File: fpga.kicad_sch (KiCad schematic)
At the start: 0 parts

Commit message: Chose amplifiers
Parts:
- added U10: P0082_TOPMOUNT, P0082_TOPMOUNT:MODULE_P0082_TOPMOUNT, symbol P0082_TOPMOUNT:P0082_TOPMOUNT
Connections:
- new net: U10.S1 (SHIELD), U10.S2 (SHIELD), U10.S3 (SHIELD), U10.S4 (SHIELD)

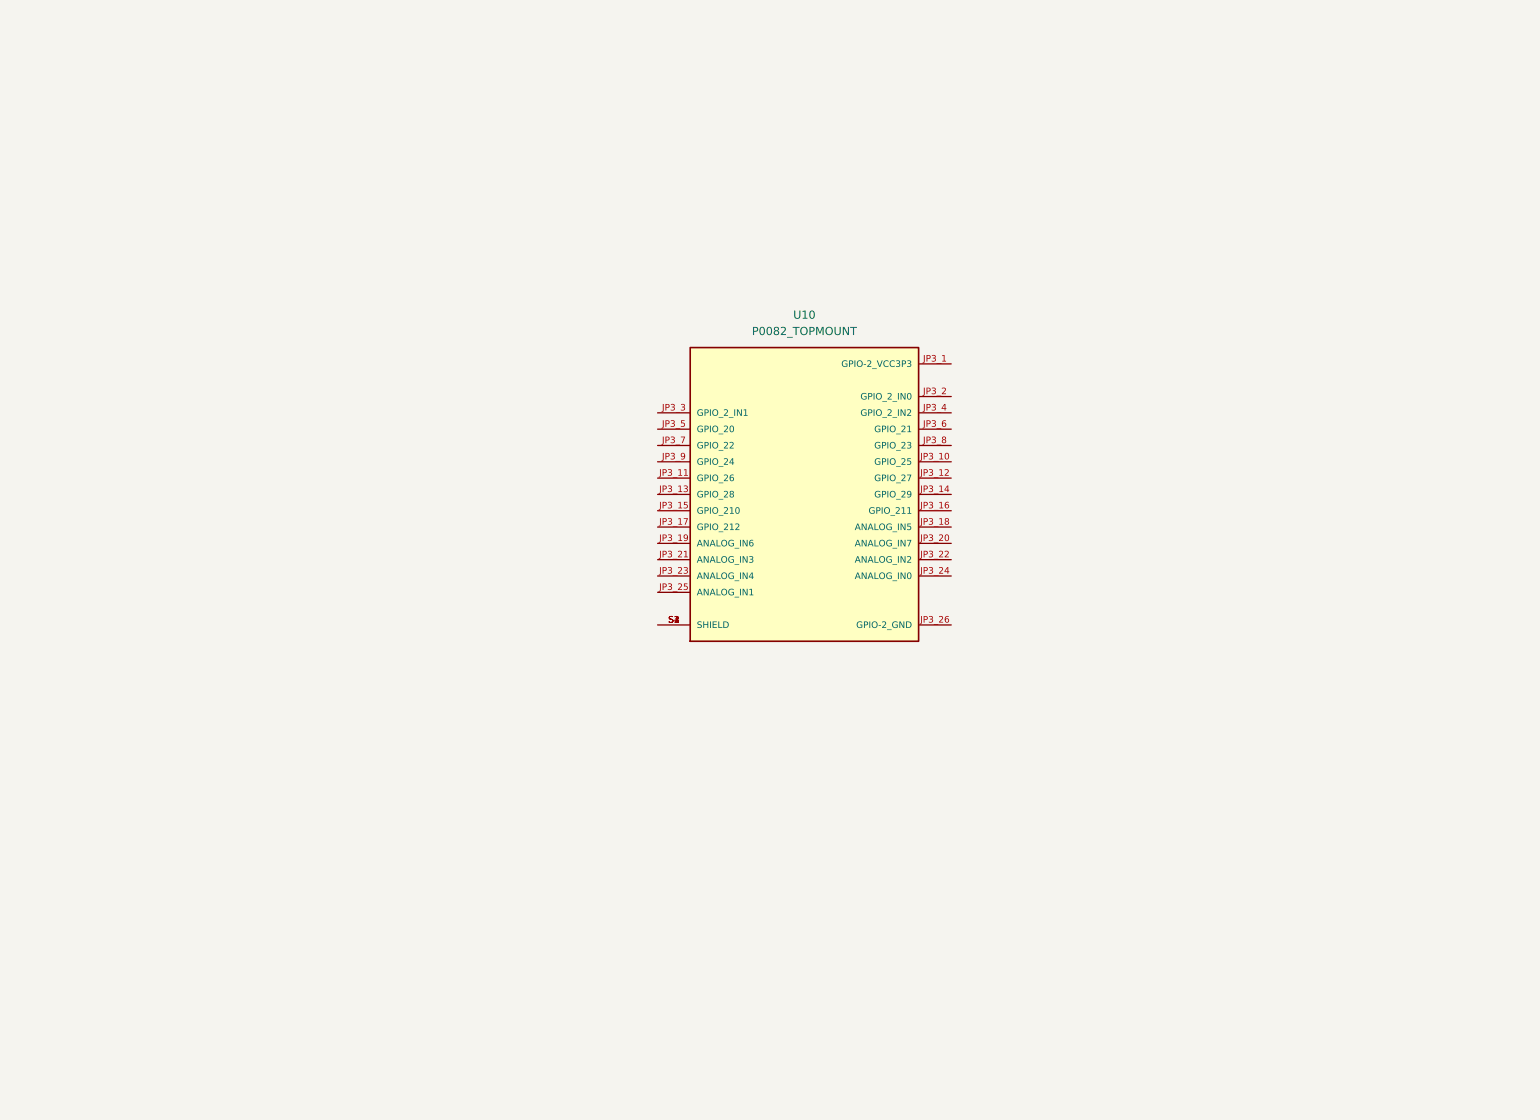
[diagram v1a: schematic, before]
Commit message: Add some of the AF power supply levels
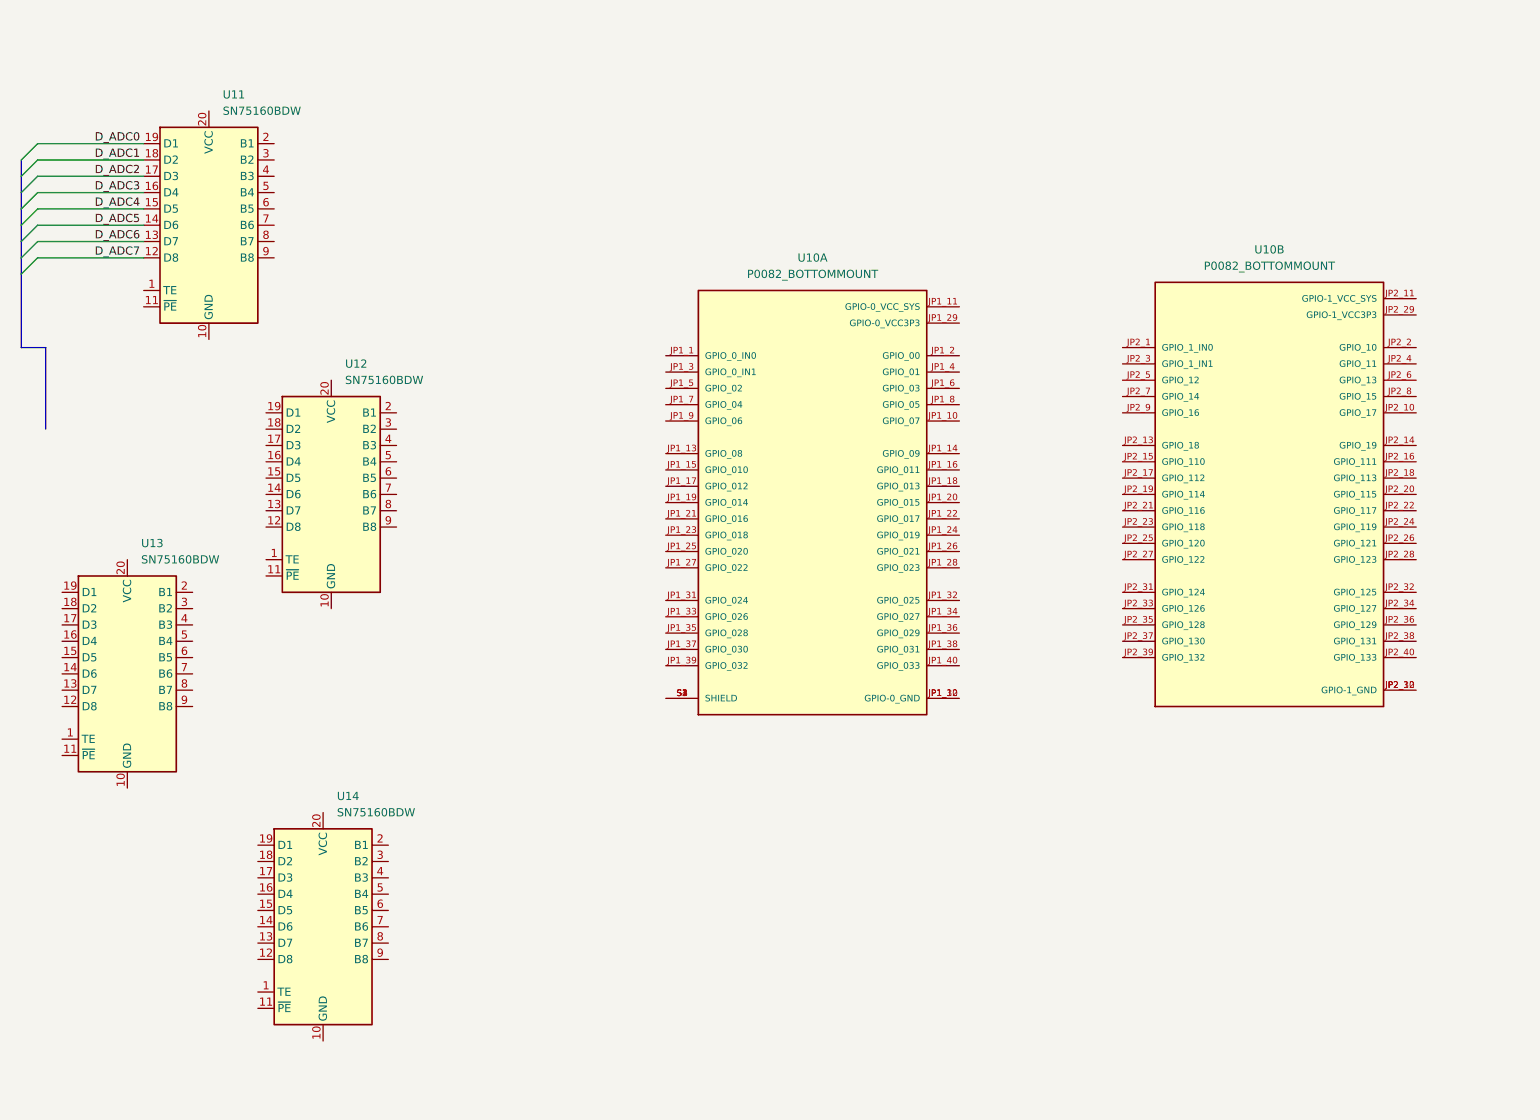
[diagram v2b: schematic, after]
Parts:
- removed U10: P0082_TOPMOUNT, P0082_TOPMOUNT:MODULE_P0082_TOPMOUNT, symbol P0082_TOPMOUNT:P0082_TOPMOUNT
- added U10: P0082_BOTTOMMOUNT, P0082_BOTTOMMOUNT:MODULE_P0082_BOTTOMMOUNT, symbol P0082_BOTTOMMOUNT:P0082_BOTTOMMOUNT
- added U11, U12, U13, U14: SN75160BDW, Package_SO:SOIC-20W_7.5x12.8mm_P1.27mm, symbol Interface:SN75160BDW
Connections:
- new net: U10.JP1_12 (GPIO-0_GND), U10.JP1_30 (GPIO-0_GND)
- new net: U10.S1 (SHIELD), U10.S2 (SHIELD), U10.S3 (SHIELD), U10.S4 (SHIELD)
- new net: U10.JP2_12 (GPIO-1_GND), U10.JP2_30 (GPIO-1_GND)
- new net D_ADC0: U11.19 (D1)
- new net D_ADC1: U11.18 (D2)
- new net D_ADC2: U11.17 (D3)
- new net D_ADC3: U11.16 (D4)
- new net D_ADC4: U11.15 (D5)
- new net D_ADC5: U11.14 (D6)
- new net D_ADC6: U11.13 (D7)
- new net D_ADC7: U11.12 (D8)

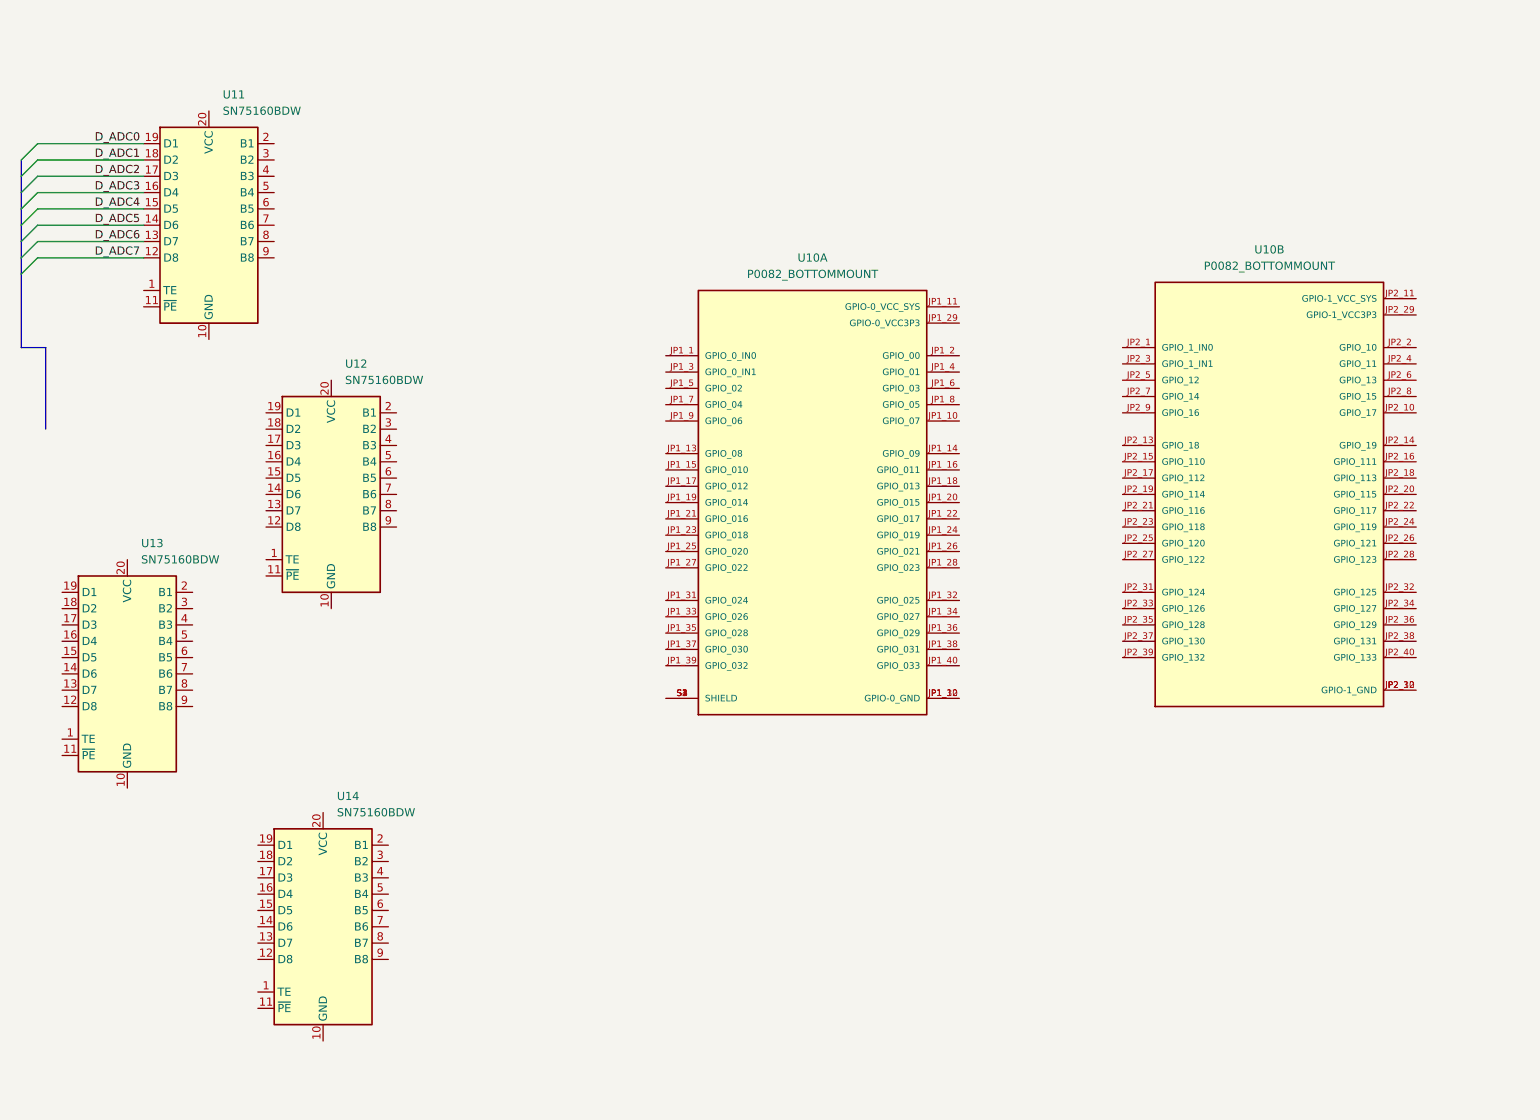
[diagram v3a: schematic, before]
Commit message: Link up ADC to FPGA
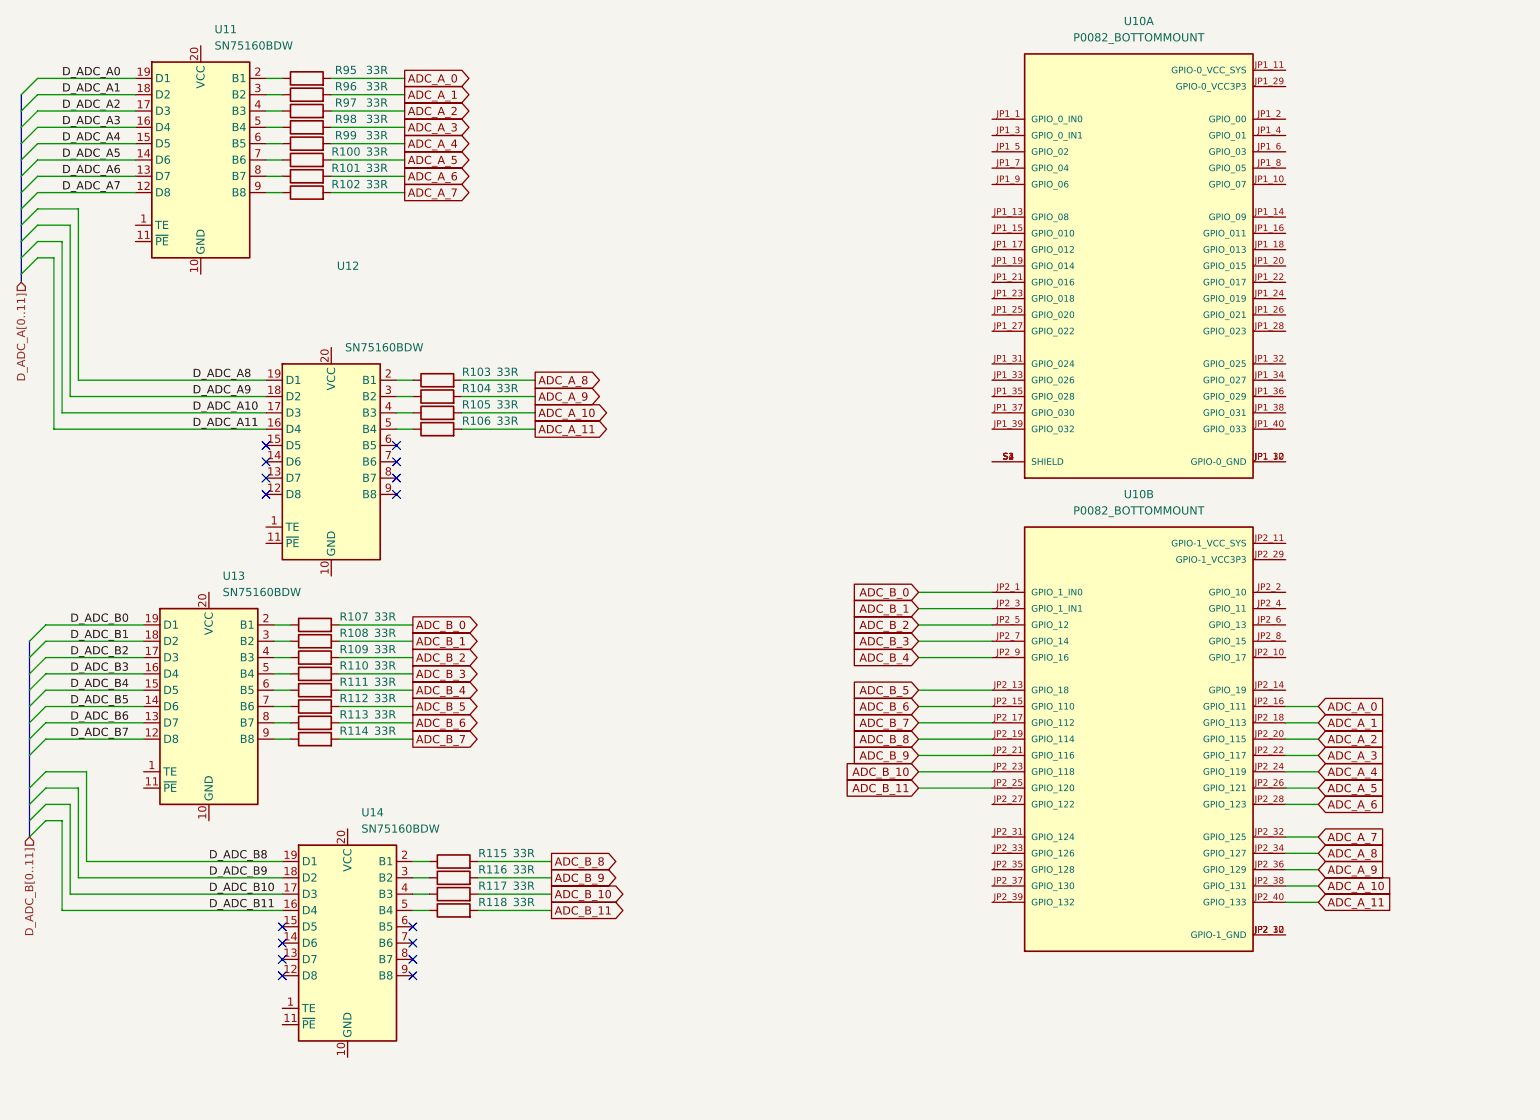
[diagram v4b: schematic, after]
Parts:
- added R100, R101, R102, R103, R104, R105, R106, R107, R108, R109, R110, R111, R112, R113, R114, R115, R116, R117, R118, R95, R96, R97, R98, R99: 33R, Resistor_SMD:R_0402_1005Metric_Pad0.72x0.64mm_HandSolder, symbol Device:R
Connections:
- net D_ADC_A11: now reaches U12.16 (D4)
- net D_ADC_A10: now reaches U12.17 (D3)
- net D_ADC_A9: now reaches U12.18 (D2)
- net D_ADC_A8: now reaches U12.19 (D1)
- net at U12.2 (B1): now also R103.1
- net at U12.3 (B2): now also R104.1
- net at U12.4 (B3): now also R105.1
- net at U12.5 (B4): now also R106.1
- net at U11.2 (B1): now also R95.1
- net at U11.3 (B2): now also R96.1
- net at U11.4 (B3): now also R97.1
- net at U11.5 (B4): now also R98.1
- net at U11.6 (B5): now also R99.1
- net at U11.7 (B6): now also R100.1
- net at U11.8 (B7): now also R101.1
- net at U11.9 (B8): now also R102.1
- net D_ADC_B7: now reaches U13.12 (D8)
- net D_ADC_B6: now reaches U13.13 (D7)
- net D_ADC_B5: now reaches U13.14 (D6)
- net D_ADC_B4: now reaches U13.15 (D5)
- net D_ADC_B3: now reaches U13.16 (D4)
- net D_ADC_B2: now reaches U13.17 (D3)
- net D_ADC_B1: now reaches U13.18 (D2)
- net D_ADC_B0: now reaches U13.19 (D1)
- net at U13.2 (B1): now also R107.1
- net at U13.3 (B2): now also R108.1
- net at U13.4 (B3): now also R109.1
- net at U13.5 (B4): now also R110.1
- net at U13.6 (B5): now also R111.1
- net at U13.7 (B6): now also R112.1
- net at U13.8 (B7): now also R113.1
- net at U13.9 (B8): now also R114.1
- net D_ADC_B11: now reaches U14.16 (D4)
- net D_ADC_B10: now reaches U14.17 (D3)
- net D_ADC_B9: now reaches U14.18 (D2)
- net D_ADC_B8: now reaches U14.19 (D1)
- net at U14.2 (B1): now also R115.1
- net at U14.3 (B2): now also R116.1
- net at U14.4 (B3): now also R117.1
- net at U14.5 (B4): now also R118.1
- net ADC_B_0: now reaches U10.JP2_1 (GPIO_1_IN0)
- net ADC_B_0: now also R107.2
- net ADC_B_5: now reaches U10.JP2_13 (GPIO_18)
- net ADC_B_5: now also R112.2
- net ADC_B_6: now reaches U10.JP2_15 (GPIO_110)
- net ADC_B_6: now also R113.2
- net ADC_A_0: now reaches U10.JP2_16 (GPIO_111)
- net ADC_A_0: now also R95.2
- net ADC_B_7: now reaches U10.JP2_17 (GPIO_112)
- net ADC_B_7: now also R114.2
- net ADC_A_1: now reaches U10.JP2_18 (GPIO_113)
- net ADC_A_1: now also R96.2
- net ADC_B_8: now reaches U10.JP2_19 (GPIO_114)
- net ADC_B_8: now also R115.2
- net ADC_A_2: now reaches U10.JP2_20 (GPIO_115)
- net ADC_A_2: now also R97.2
- net ADC_B_9: now reaches U10.JP2_21 (GPIO_116)
- net ADC_B_9: now also R116.2
- net ADC_A_3: now reaches U10.JP2_22 (GPIO_117)
- net ADC_A_3: now also R98.2
- net ADC_B_10: now reaches U10.JP2_23 (GPIO_118)
- net ADC_B_10: now also R117.2
- net ADC_A_4: now reaches U10.JP2_24 (GPIO_119)
- net ADC_A_4: now also R99.2
- net ADC_B_11: now reaches U10.JP2_25 (GPIO_120)
- net ADC_B_11: now also R118.2
- net ADC_A_5: now reaches U10.JP2_26 (GPIO_121)
- net ADC_A_5: now also R100.2
- net ADC_A_6: now reaches U10.JP2_28 (GPIO_123)
- net ADC_A_6: now also R101.2
- net ADC_B_1: now reaches U10.JP2_3 (GPIO_1_IN1)
- net ADC_B_1: now also R108.2
- net ADC_A_7: now reaches U10.JP2_32 (GPIO_125)
- net ADC_A_7: now also R102.2
- net ADC_A_8: now reaches U10.JP2_34 (GPIO_127)
- net ADC_A_8: now also R103.2
- net ADC_A_9: now reaches U10.JP2_36 (GPIO_129)
- net ADC_A_9: now also R104.2
- net ADC_A_10: now reaches U10.JP2_38 (GPIO_131)
- net ADC_A_10: now also R105.2
- net ADC_A_11: now reaches U10.JP2_40 (GPIO_133)
- net ADC_A_11: now also R106.2
- net ADC_B_2: now reaches U10.JP2_5 (GPIO_12)
- net ADC_B_2: now also R109.2
- net ADC_B_3: now reaches U10.JP2_7 (GPIO_14)
- net ADC_B_3: now also R110.2
- net ADC_B_4: now reaches U10.JP2_9 (GPIO_16)
- net ADC_B_4: now also R111.2
- net D_ADC0 renamed D_ADC_A0
- net D_ADC1 renamed D_ADC_A1
- net D_ADC2 renamed D_ADC_A2
- net D_ADC3 renamed D_ADC_A3
- net D_ADC4 renamed D_ADC_A4
- net D_ADC5 renamed D_ADC_A5
- net D_ADC6 renamed D_ADC_A6
- net D_ADC7 renamed D_ADC_A7
- no-connect marks 0 -> 16
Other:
- moved on the sheet: U10A, U10B, U11, U12

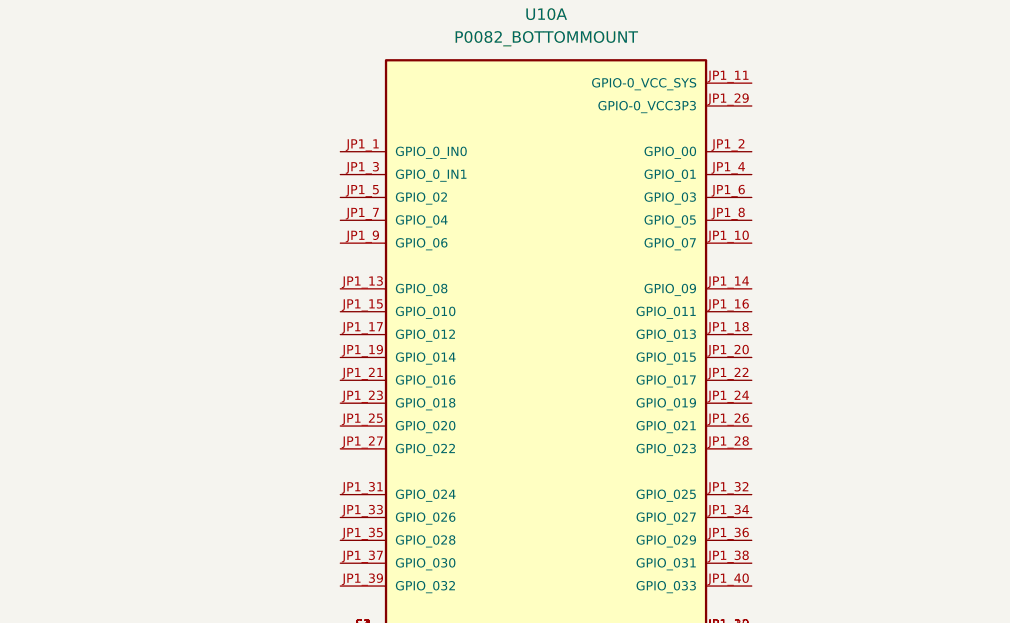
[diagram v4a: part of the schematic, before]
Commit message: Add connection between MCU and FPGA
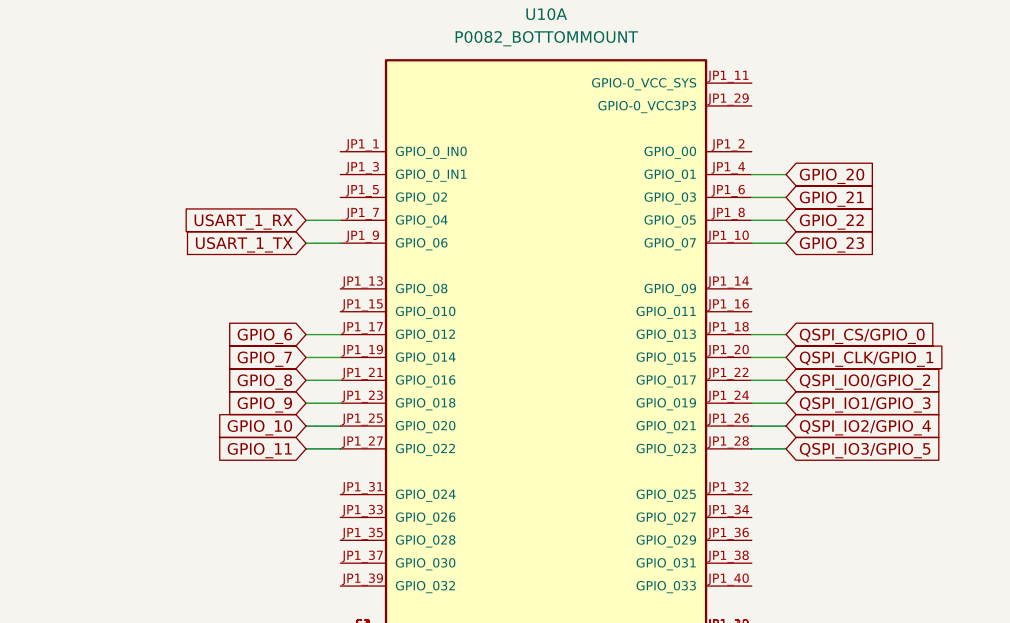
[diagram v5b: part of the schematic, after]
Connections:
- net GPIO_23: now reaches U10.JP1_10 (GPIO_07)
- net GPIO_6: now reaches U10.JP1_17 (GPIO_012)
- net QSPI_CS/GPIO_0: now reaches U10.JP1_18 (GPIO_013)
- net GPIO_7: now reaches U10.JP1_19 (GPIO_014)
- net QSPI_CLK/GPIO_1: now reaches U10.JP1_20 (GPIO_015)
- net GPIO_8: now reaches U10.JP1_21 (GPIO_016)
- net QSPI_IO0/GPIO_2: now reaches U10.JP1_22 (GPIO_017)
- net GPIO_9: now reaches U10.JP1_23 (GPIO_018)
- net QSPI_IO1/GPIO_3: now reaches U10.JP1_24 (GPIO_019)
- net GPIO_10: now reaches U10.JP1_25 (GPIO_020)
- net QSPI_IO2/GPIO_4: now reaches U10.JP1_26 (GPIO_021)
- net GPIO_11: now reaches U10.JP1_27 (GPIO_022)
- net QSPI_IO3/GPIO_5: now reaches U10.JP1_28 (GPIO_023)
- net GPIO_20: now reaches U10.JP1_4 (GPIO_01)
- net GPIO_21: now reaches U10.JP1_6 (GPIO_03)
- net USART_1_RX: now reaches U10.JP1_7 (GPIO_04)
- net GPIO_22: now reaches U10.JP1_8 (GPIO_05)
- net USART_1_TX: now reaches U10.JP1_9 (GPIO_06)
